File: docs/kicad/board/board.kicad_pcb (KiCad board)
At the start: 2 copper layers, 17 parts, among them J1 VIN, J10 WHEEL_4, J11 FLAG, J12 LED, J13 COMPASS, J14 SWITCH, J2 LEFT, J3 RIGHT, J4 UNUSED, J5 ARM, J6 LID, J7 WHEEL_1, J8 WHEEL_2, J9 WHEEL_3, SW1 BUTTON_1, SW2 BUTTON_2, U1 ARDUINO_NANO

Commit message: Built version 2 for Daniel
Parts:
- removed J4: UNUSED, cnc3018-PCB:my4pin
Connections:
- U1 pad 12: U_IR -> Net-(U1-Pad12)
- U1 pad 15: U_SENS -> Net-(U1-Pad15)
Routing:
- net +5V: track 90.4 -> 72.6 mm, vias 4 -> 2
- net U_IR: track 12.3 -> 0.00 mm
- net U_SENS: track 10.2 -> 0.00 mm
- net L_IR: track 25.2 -> 27.0 mm, vias 1 -> 2
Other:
- board outline added: 62 x 53 mm

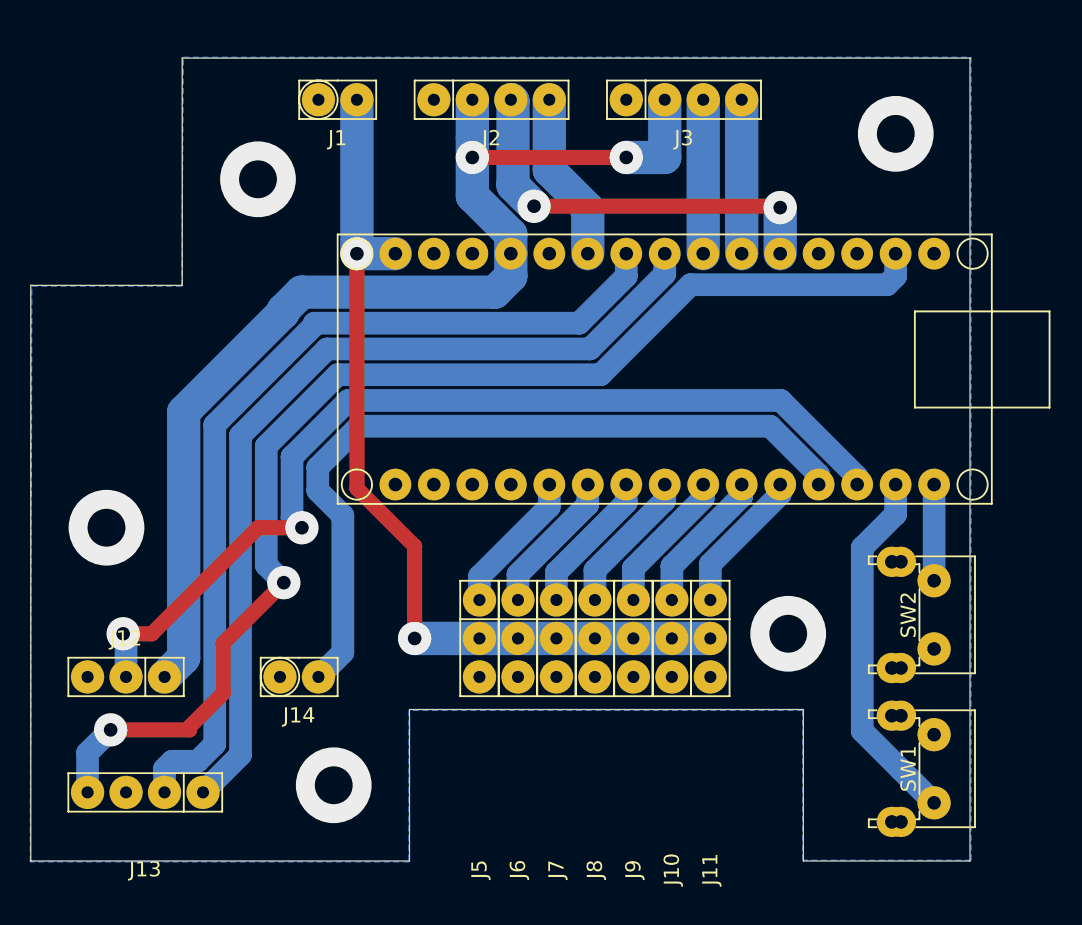
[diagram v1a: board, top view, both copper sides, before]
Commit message: created 3D rendering of PCB with my new kicad footprint files
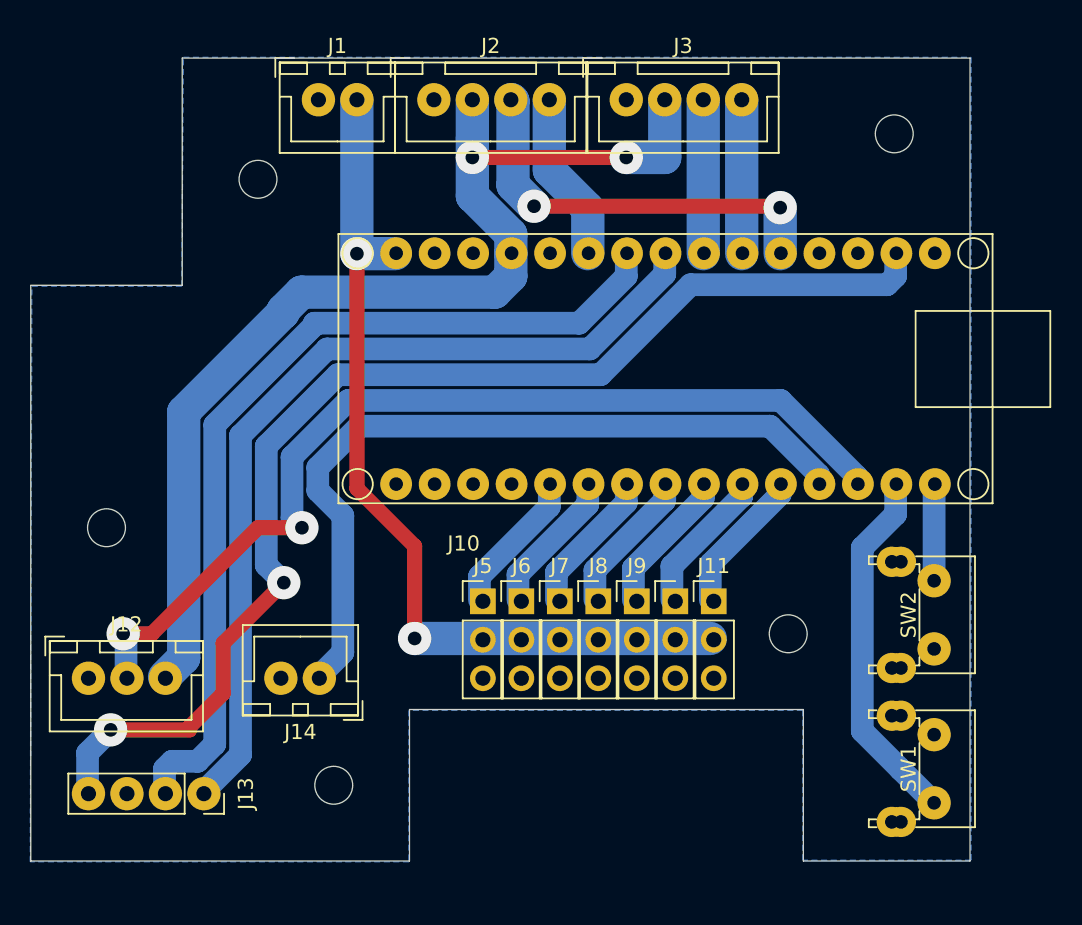
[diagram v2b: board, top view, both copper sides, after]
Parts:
- added REF**: myMountingHole_2.5mm, 0_my_footprints:myMountingHole_2.5mm, F.Cu at (20.0, -5.00)
- added REF**: myMountingHole_2.5mm, 0_my_footprints:myMountingHole_2.5mm, F.Cu at (50.0, -15.0)
- added REF**: myMountingHole_2.5mm, 0_my_footprints:myMountingHole_2.5mm, F.Cu at (57.0, -48.0)
- added REF**: myMountingHole_2.5mm, 0_my_footprints:myMountingHole_2.5mm, F.Cu at (15.0, -45.0)
- added REF**: myMountingHole_2.5mm, 0_my_footprints:myMountingHole_2.5mm, F.Cu at (5.00, -22.0)
- J1, J14: footprint cnc3018-PCB:my2pin -> 0_my_footprints:myJSTx02
- J10, J11, J5, J6, J7, J8, J9: footprint cnc3018-PCB:my3pin -> Connector_PinHeader_2.54mm:PinHeader_1x03_P2.54mm_Vertical
- J12: footprint cnc3018-PCB:my3pin -> 0_my_footprints:myJSTx03
- J13: footprint cnc3018-PCB:my4pin -> 0_my_footprints:myPinSocket_1x04
- J2, J3: footprint cnc3018-PCB:my4pin -> 0_my_footprints:myJSTx04
- SW1, SW2: footprint cnc3018-PCB:right_angle_button -> 0_my_footprints:myButtonAngled
- U1: footprint cnc3018-PCB:ARDUINO_NANO -> 0_my_footprints:myArduinoNano
- moved J14 2.60 mm to (19.1, -12.1), turned to 180 degrees
- moved J12 2.48 mm to (3.81, -12.1), turned to 0 degrees
- moved J10 2.47 mm to (42.5, -17.1), turned to 0 degrees
- moved J11 2.47 mm to (45.1, -17.1), turned to 0 degrees
- moved J6 2.47 mm to (32.4, -17.1), turned to 0 degrees
- moved J8 2.47 mm to (37.5, -17.1), turned to 0 degrees
- moved J9 2.47 mm to (40.0, -17.1), turned to 0 degrees
- moved J5 2.47 mm to (29.8, -17.1), turned to 0 degrees
- moved J7 2.47 mm to (34.9, -17.1), turned to 0 degrees
- moved J13 0.10 mm to (11.4, -4.45), turned to 270 degrees
- moved U1 0.06 mm to (41.9, -32.5)
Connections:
- J12 pad 1: +5V -> GND
- J12 pad 3: GND -> +5V
- J14 pad 1: GND -> SWITCH
- J14 pad 2: SWITCH -> GND
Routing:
- net GND: vias 5 -> 0

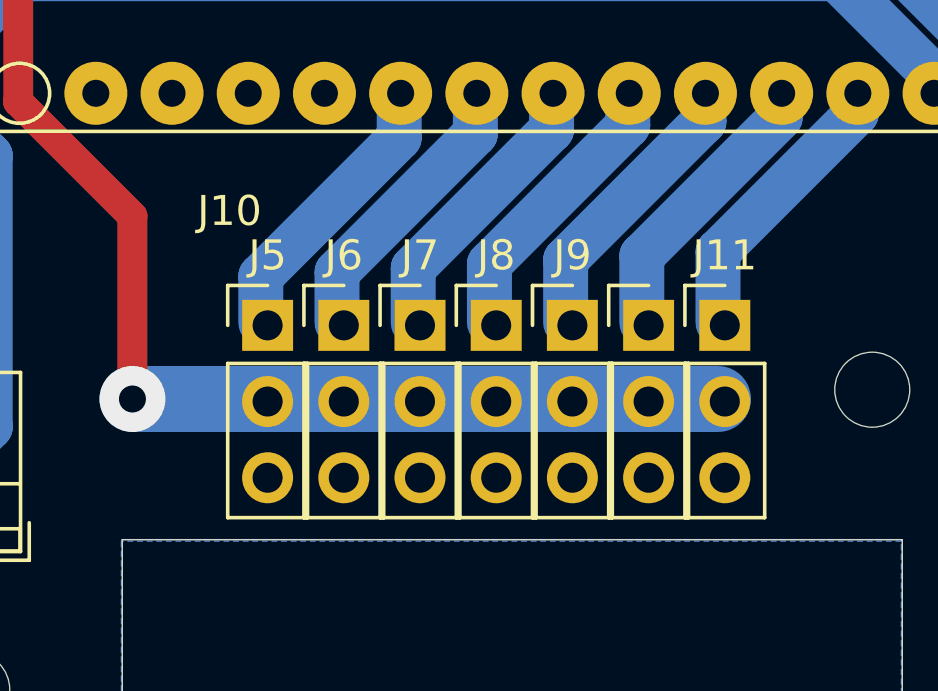
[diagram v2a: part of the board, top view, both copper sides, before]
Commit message: commit new board schematic using my new symbols and 3D footprints
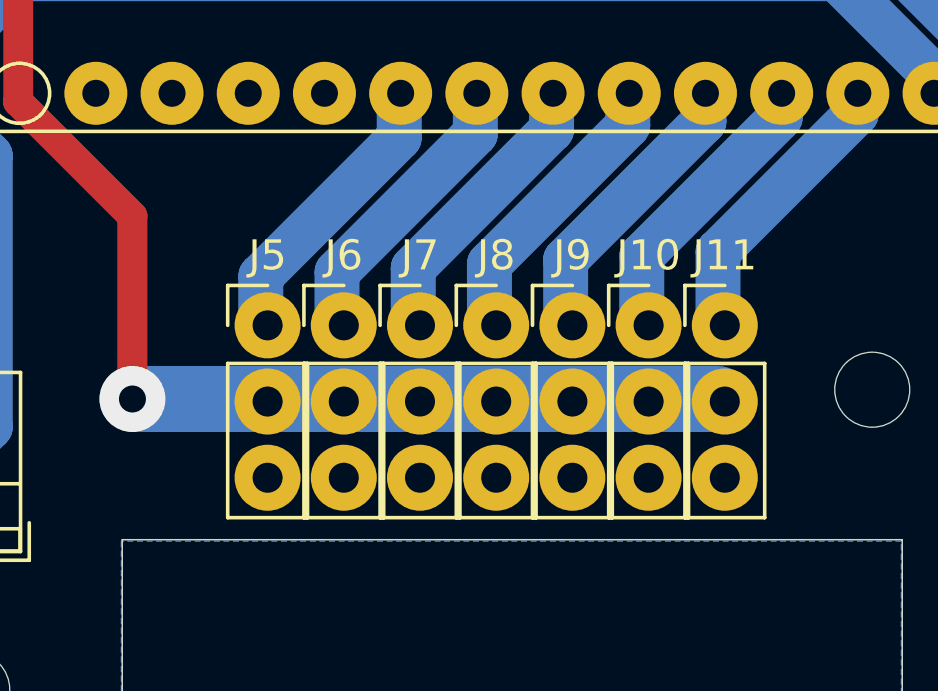
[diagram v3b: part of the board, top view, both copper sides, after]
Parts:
- J10, J11, J5, J6, J7, J8, J9: footprint Connector_PinHeader_2.54mm:PinHeader_1x03_P2.54mm_Vertical -> 0_my_footprints:myPinHeader_1x03

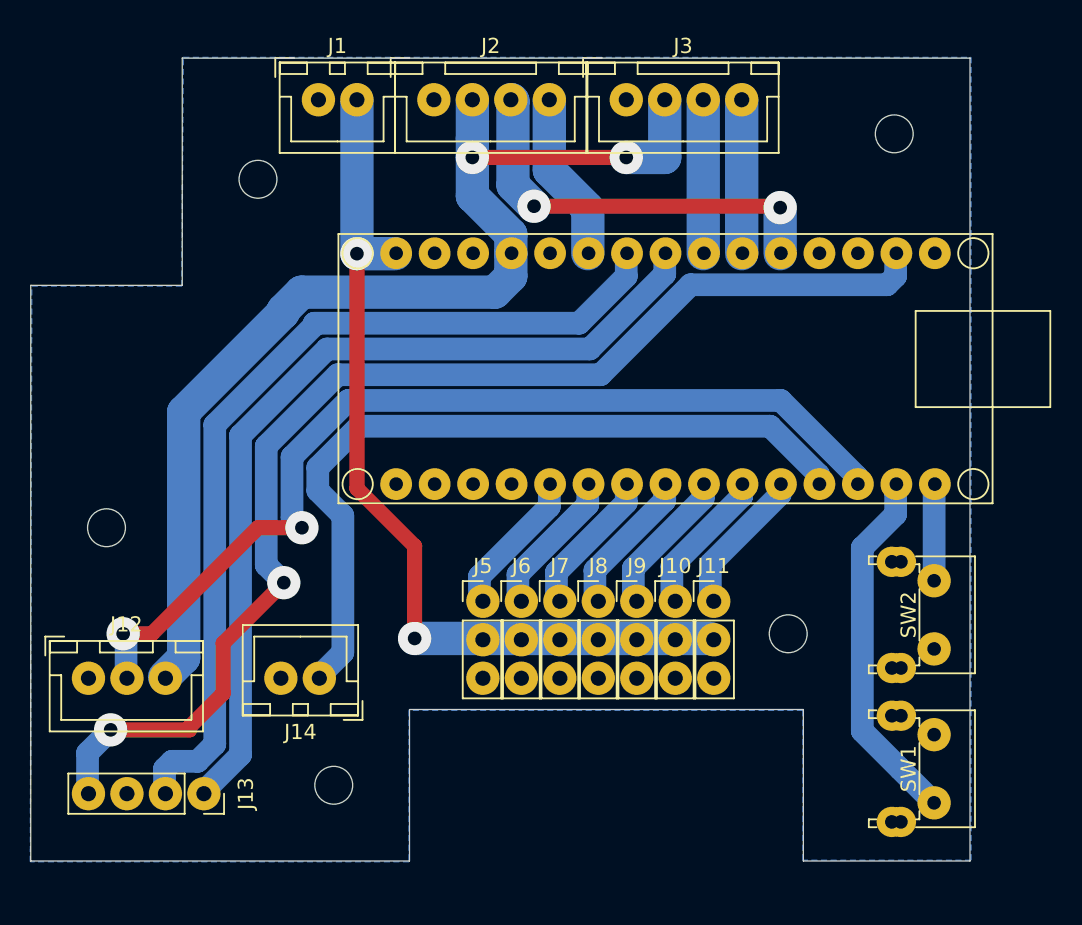
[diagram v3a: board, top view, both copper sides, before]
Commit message: SIMPLIFY: got rid of buttons and compass, smaller PCB, all new outputs
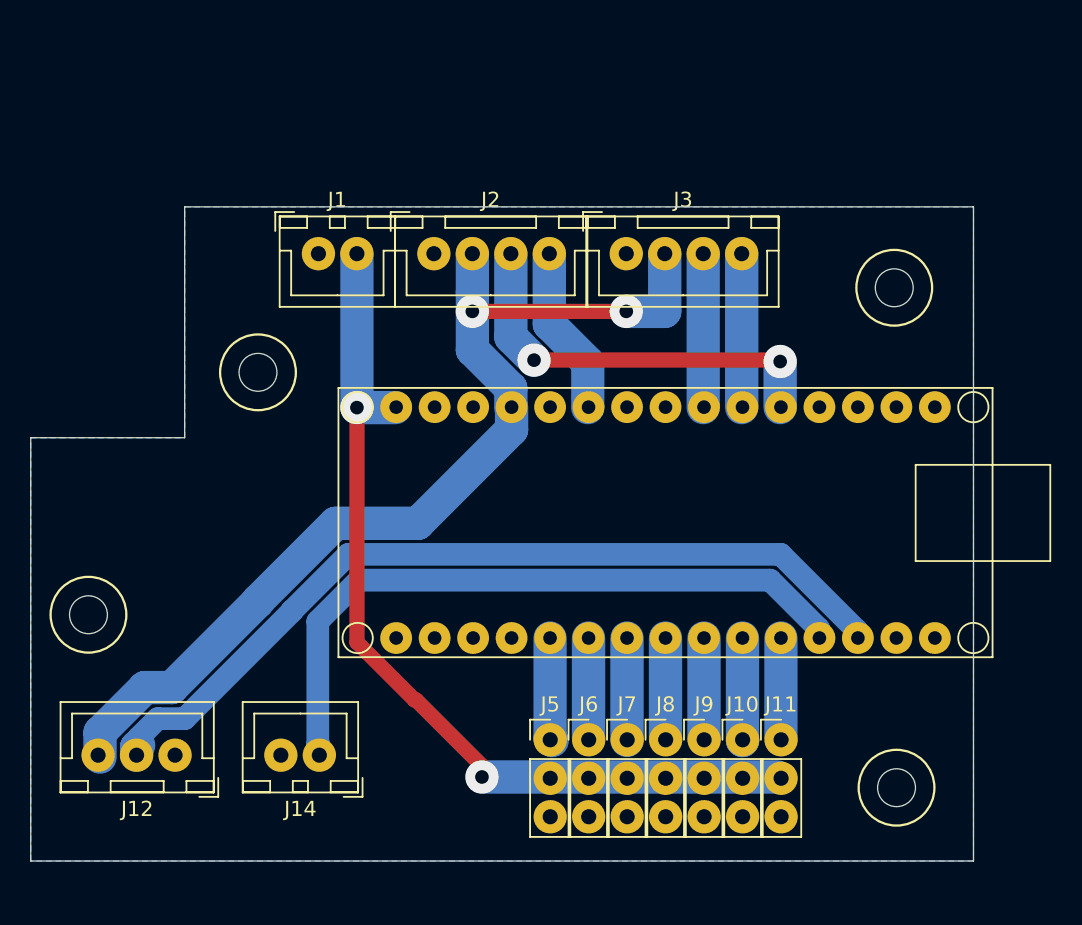
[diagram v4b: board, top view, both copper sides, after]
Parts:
- removed J13: COMPASS, 0_my_footprints:myPinSocket_1x04
- removed the REF** at (20.0, -5.00)
- removed the REF** at (50.0, -15.0)
- removed the REF** at (57.0, -48.0)
- removed the REF** at (15.0, -45.0)
- removed the REF** at (5.00, -22.0)
- removed SW1: BUTTON_1, 0_my_footprints:myButtonAngled
- removed SW2: BUTTON_2, 0_my_footprints:myButtonAngled
- added REF**: myMountingHole_2.5mm, 0_my_footprints:myMountingHole_2.5mm, F.Cu at (57.1, -4.84)
- added REF**: myMountingHole_2.5mm, 0_my_footprints:myMountingHole_2.5mm, F.Cu at (57.0, -37.8)
- added REF**: myMountingHole_2.5mm, 0_my_footprints:myMountingHole_2.5mm, F.Cu at (15.0, -32.3)
- added REF**: myMountingHole_2.5mm, 0_my_footprints:myMountingHole_2.5mm, F.Cu at (3.81, -16.3)
- moved J10 10.2 mm to (47.0, -8.00)
- moved J11 10.2 mm to (49.5, -8.00)
- moved J5 10.2 mm to (34.3, -8.00)
- moved J6 10.2 mm to (36.8, -8.00)
- moved J7 10.2 mm to (39.4, -8.00)
- moved J9 10.2 mm to (44.5, -8.00)
- moved J8 10.2 mm to (41.9, -8.00)
- moved U1 10.2 mm to (41.9, -22.3)
- moved J1 10.2 mm to (19.0, -40.1)
- moved J2 10.2 mm to (26.6, -40.1)
- moved J3 10.2 mm to (39.3, -40.1)
- moved J12 7.65 mm to (9.53, -6.99), turned to 180 degrees
- moved J14 5.08 mm to (19.1, -6.99)
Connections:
- U1 pad 14: +3V3 -> Net-(U1-Pad14)
- U1 pad 16: BUT_2 -> GND
- U1 pad 17: BUT_1 -> GND
- U1 pad 7: SCL -> GND
- U1 pad 8: SDA -> GND
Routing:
- net +3V3: track 79.4 -> 0.00 mm, vias 2 -> 0
- net SCL: track 59.9 -> 0.00 mm
- net SDA: track 58.3 -> 0.00 mm
- net BUT_1: track 24.4 -> 0.00 mm
- net LED: track 64.2 -> 57.1 mm, vias 2 -> 0
- net SWITCH: track 51.8 -> 44.8 mm
- net BUT_2: track 6.35 -> 0.00 mm
- net +5V: track 72.6 -> 66.3 mm
- net FLAG: track 9.66 -> 6.71 mm
- net LID: track 9.53 -> 6.63 mm
- net WHEEL_2: track 9.65 -> 6.76 mm
- net WHEEL_3: track 10.2 -> 7.31 mm
- net WHEEL_1: track 9.53 -> 6.76 mm
- net WHEEL_4: track 9.53 -> 6.78 mm
- net ARM: track 9.57 -> 6.87 mm
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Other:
- board size 62 x 53 mm -> 62.2 x 43.2 mm
